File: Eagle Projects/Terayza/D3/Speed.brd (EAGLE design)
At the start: 100 x 80 mm, 16 parts, among them U1 ATMEGA328P-AU

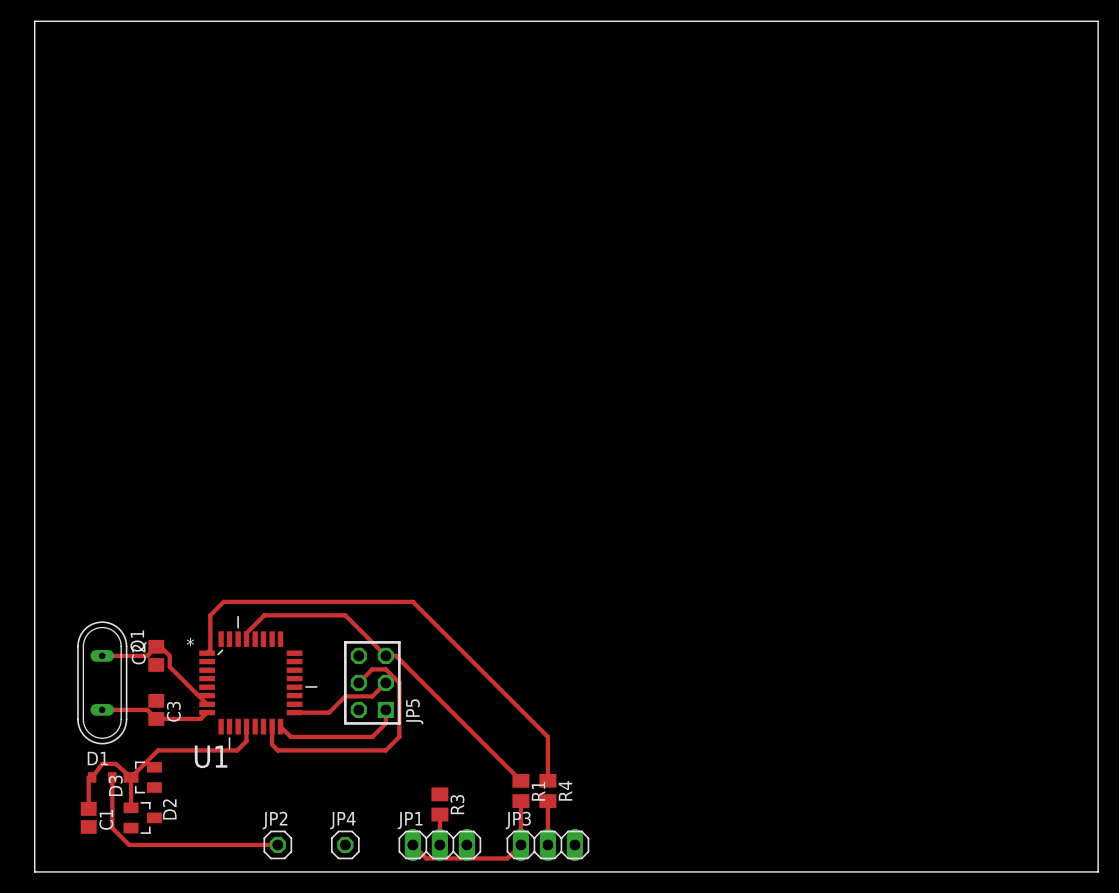
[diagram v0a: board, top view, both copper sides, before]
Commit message: Added CAN I/O, Connectors, SMPS block to T's Speed Board
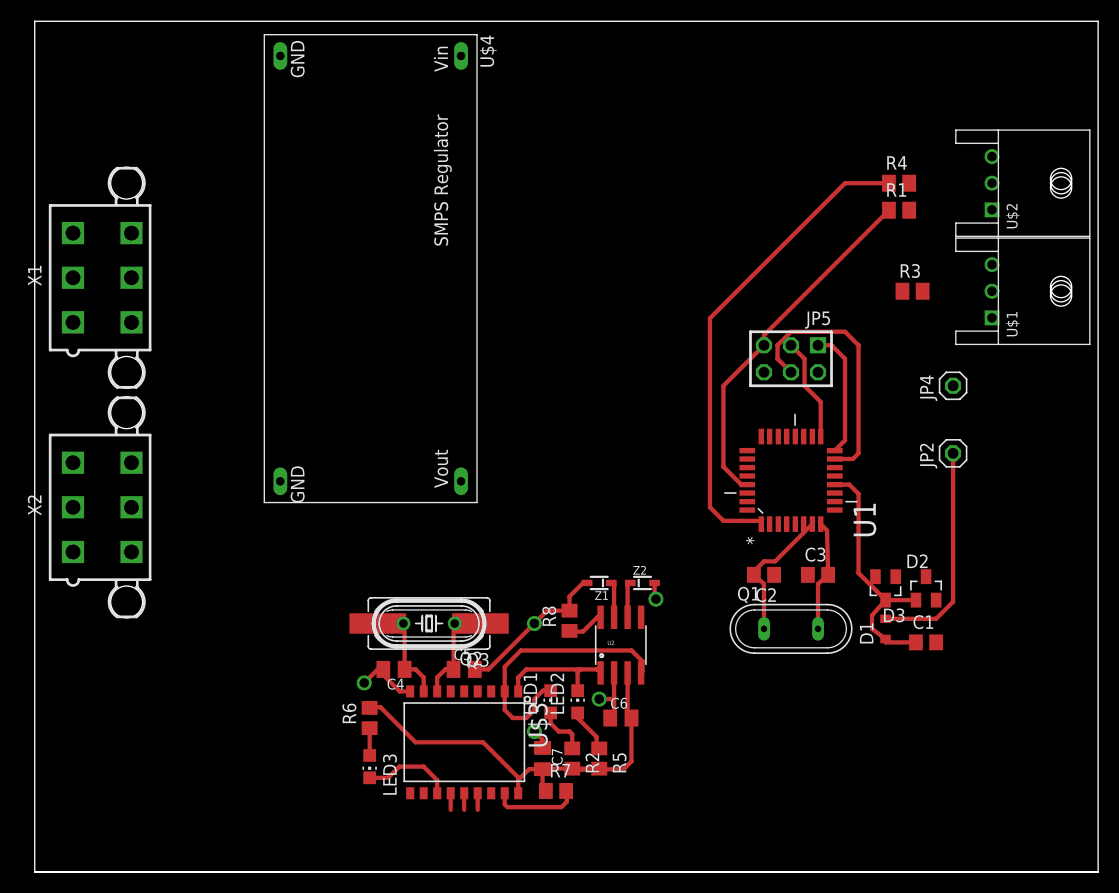
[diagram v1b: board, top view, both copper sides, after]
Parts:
- removed JP1, JP3: (no value), pinhead:1X03
- added C4, C5: 22pF, resistor:C0805K
- added C6, C7: 100nF, resistor:C0805K
- added LED1: RX, led:CHIP-LED0805
- added LED2: TX, led:CHIP-LED0805
- added LED3: INT, led:CHIP-LED0805
- added Q2: 16MHz, crystal:HC49/S
- added Q3: 16MHz, crystal:HC49UP
- added R2, R5, R6: 1k, resistor:R0805
- added R7, R8: 100k, resistor:R0805
- added U$1, U$2: HEADER-3WAY, con-TE-EP:1744426-3
- added U$3: MCP2515SO, RobThePyro:SO-18W
- added U$4: SMPSBOARD, RobThePyro:SMPSBOARD
- added U2: MCP2551, SparkFun:SO08
- added X1, X2: 5566-6, con-molex:5566-6
- added Z1, Z2: TVS-UD-SOD323, supressor:SOD323
- moved C1 80.5 mm to (83.8, 21.6), turned to 0 degrees
- moved D2 76.8 mm to (83.8, 26.7), turned to 0 degrees
- moved D1 75.0 mm to (80.0, 22.9), turned to 90 degrees
- moved JP2 73.4 mm to (86.4, 39.4), turned to 90 degrees
- moved D3 72.1 mm to (80.0, 26.7), turned to 180 degrees
- moved JP4 71.6 mm to (86.4, 45.7), turned to 90 degrees
- moved R4 66.0 mm to (81.3, 64.8), turned to 0 degrees
- moved R3 65.6 mm to (82.5, 54.6), turned to 0 degrees
- moved R1 65.2 mm to (81.3, 62.2), turned to 0 degrees
- moved Q1 65.0 mm to (71.1, 22.9), turned to 0 degrees
- moved C3 63.5 mm to (73.7, 27.9), turned to 0 degrees
- moved C2 57.7 mm to (68.6, 27.9), turned to 180 degrees
- moved U1 54.3 mm to (71.1, 36.8), turned to 90 degrees
- moved JP5 49.8 mm to (71.1, 48.3), turned to 180 degrees
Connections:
- removed net N$10: JP1.2, R3.2
- removed net N$13: JP3.2, R4.2
- new net +5V: C6.2, C7.2, R2.2, R5.2, R6.2, R7.1, U$3.18, U2.3
- new net CANCS: U$3.16
- new net CANH: U2.7, X1.1, X2.1, Z1.C
- new net CANINT: LED3.C, U$3.12
- new net CANL: U2.6, X1.4, X2.4, Z2.C
- new net CANRST: R7.2, U$3.17
- new net CANSTBY: R8.1, U2.8
- new net MISO: U$3.15
- new net MOSI: U$3.14
- new net N$15: LED1.A, R2.1
- new net N$16: LED2.A, R5.1
- new net N$17: LED3.A, R6.1
- new net N$18: C4.1, Q2.2, Q3.2, U$3.8
- new net N$19: C5.1, Q2.1, Q3.1, U$3.7
- new net PD2: R3.1, R3.2, U$1.P$2, U1.32
- new net PD3: R4.1, R4.2, U$2.P$2, U1.1
- new net RXCAN: LED1.C, U$3.2, U2.4
- new net SCK: U$3.13
- new net SPARE1: X1.5, X2.5
- new net SPARE2: X1.6, X2.6
- new net TXCAN: LED2.C, U$3.1, U2.1
- new net VIN: X1.3, X2.3
- net GND: now also C4.2, C5.2, C6.1, C7.1, R8.2, U$1.P$1, U$2.P$1, U$3.9, U$4.GND, U$4.GND@, U2.2, X1.2, X2.2, Z1.A, Z2.A; no longer JP1.3, JP3.3
- net N$11: now also U$4.VIN; no longer R3.1, U1.32
- net N$12: now also U$4.VOUT; no longer R4.1, U1.1
- net VCC: now also U$1.P$3, U$2.P$3; no longer JP1.1, JP3.1
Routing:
- net N$12: track 45.3 -> 0.00 mm
- net PD3: track 0.00 -> 44.9 mm
- net +5V: track 0.00 -> 44.2 mm
- net GND: track 0.00 -> 29.6 mm, vias 0 -> 5
- net RXCAN: track 0.00 -> 25.5 mm
- net VCC: track 15.3 -> 0.00 mm
- net TXCAN: track 0.00 -> 11.6 mm
- net N$18: track 0.00 -> 10.3 mm
- net N$19: track 0.00 -> 10.0 mm
- net CANINT: track 0.00 -> 8.54 mm
- net CANRST: track 0.00 -> 8.26 mm
- net N$15: track 0.00 -> 4.77 mm
- net N$16: track 0.00 -> 4.18 mm
- net N$13: track 4.13 -> 0.00 mm
- net CANSTBY: track 0.00 -> 3.51 mm
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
